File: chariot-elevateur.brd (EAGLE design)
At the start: 123 x 78 mm, 17 parts, among them Q1 BSS138, U1 WIZ820IO

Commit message: end-of-day-commit
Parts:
- moved U1 3.16 mm to (23.0, 52.0)
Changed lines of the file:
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@@
 </layers>
 <board>
-<fusionsync huburn="a.cGVyc29uYWw6dWUyYjVjZTIy" projecturn="a.cGVyc29uYWw6dWUyYjVjZTIyIzIwMTgwOTIxMTUwMjQwNTAx" f3durn="urn:adsk.wipprod:dm.lineage:GSJ6iZW7T-ifCIeOwvPvjQ" pcbguid="b42dcfff-eba5-4b7b-b8d8-54aa01b8e055" lastpulledtime="" lastsyncedchangeguid="7340f699-62a9-14f6-8329-5ece7c968610"/>
+<fusionsync huburn="a.cGVyc29uYWw6dWUyYjVjZTIy" projecturn="a.cGVyc29uYWw6dWUyYjVjZTIyIzIwMTgwOTIxMTUwMjQwNTAx" f3durn="urn:adsk.wipprod:dm.lineage:GSJ6iZW7T-ifCIeOwvPvjQ" pcbguid="b42dcfff-eba5-4b7b-b8d8-54aa01b8e055" lastpulledtime="" lastsyncedchangeguid="24a032fd-58df-3baa-aadd-83ea89c3b94e"/>
 <plain>
 <wire x1="17.5" y1="0" x2="51.5" y2="0" width="0" layer="20"/>
@@
 <attribute name="VALUE" x="79.8" y="41" size="1.27" layer="27" font="vector"/>
 </element>
-<element name="U1" library="wiznet" package="WIZ820" value="WIZ820IO" x="20" y="53" smashed="yes" rot="R180">
-<attribute name="NAME" x="12.38" y="47.158" size="1.6764" layer="25"/>
+<element name="U1" library="wiznet" package="WIZ820" value="WIZ820IO" x="23" y="52" smashed="yes" rot="R180">
+<attribute name="NAME" x="15.38" y="46.158" size="1.6764" layer="25"/>
 </element>
 <element name="ENCODEUR_GAUCHE" library="con-jst" package="GH-04-V" value="JST-04GH-V" x="24" y="6" smashed="yes" rot="R180"/>
@@
 <contactref element="LED2" pad="C"/>
 <wire x1="86.15" y1="33.38" x2="121.71" y2="48.62" width="0" layer="19" extent="1-1"/>
-<wire x1="30.16" y1="53" x2="86.15" y2="33.38" width="0" layer="19" extent="1-1"/>
-<wire x1="30.16" y1="55.54" x2="30.16" y2="53" width="0" layer="19" extent="1-1"/>
-<wire x1="9.84" y1="53" x2="30.16" y2="53" width="0" layer="19" extent="1-1"/>
-<wire x1="33" y1="4.46" x2="9.84" y2="53" width="0" layer="19" extent="1-1"/>
+<wire x1="33.16" y1="52" x2="86.15" y2="33.38" width="0" layer="19" extent="1-1"/>
+<wire x1="33.16" y1="54.54" x2="33.16" y2="52" width="0" layer="19" extent="1-1"/>
+<wire x1="12.84" y1="52" x2="33.16" y2="52" width="0" layer="19" extent="1-1"/>
+<wire x1="33" y1="4.46" x2="12.84" y2="52" width="0" layer="19" extent="1-1"/>
 <wire x1="66.46" y1="12" x2="33" y2="4.46" width="0" layer="19" extent="1-1"/>
 <wire x1="83" y1="18.46" x2="66.46" y2="12" width="0" layer="19" extent="1-1"/>
@@
 <contactref element="U1" pad="VIN2"/>
 <contactref element="U1" pad="VIN1"/>
-<wire x1="9.84" y1="58.08" x2="9.84" y2="55.54" width="0" layer="19" extent="1-1"/>
+<wire x1="12.84" y1="57.08" x2="12.84" y2="54.54" width="0" layer="19" extent="1-1"/>
 </signal>
 <signal name="DYN_VCC">

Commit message: more components
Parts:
- added ENDSTOP: JST-03, con-jst:GH-03-V
- added FUMIGENE: DYNAMIXEL-1X03XL, 1NTech_pinhead:DYNAMIXEL_XL_1X03
- added PHARES_AR, PHARES_AV: JST-05, con-jst:GH-05-V
- added RASPBERRY: JST-06, con-jst:GH-06-V
- added TOF_AR: JST-08, con-jst:GH-08-V
- added VESC: (no value), pinhead:1X03
- moved S3 56.3 mm to (99.0, 75.0), turned to 0 degrees
- moved LED2 39.1 mm to (94.0, 64.0)
- moved LED3 39.1 mm to (94.0, 57.0)
- moved Q1 39.1 mm to (108.0, 57.0)
- moved R2 39.1 mm to (115.0, 56.0)
- moved R3 39.1 mm to (115.0, 61.0)
- moved R4 39.1 mm to (101.0, 56.0)
- moved R5 39.1 mm to (101.0, 61.0)
- moved S1 16.5 mm to (67.0, 23.0), turned to 90 degrees
- moved AX12_AV 15.0 mm to (54.0, 12.0)
- moved PAS_A_PAS 11.0 mm to (67.0, 12.0)
- moved AX12_AR 6.08 mm to (32.0, 13.0), turned to 0 degrees
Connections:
- net DYN_VCC: now also FUMIGENE.VCC
- net GND: now also FUMIGENE.GND

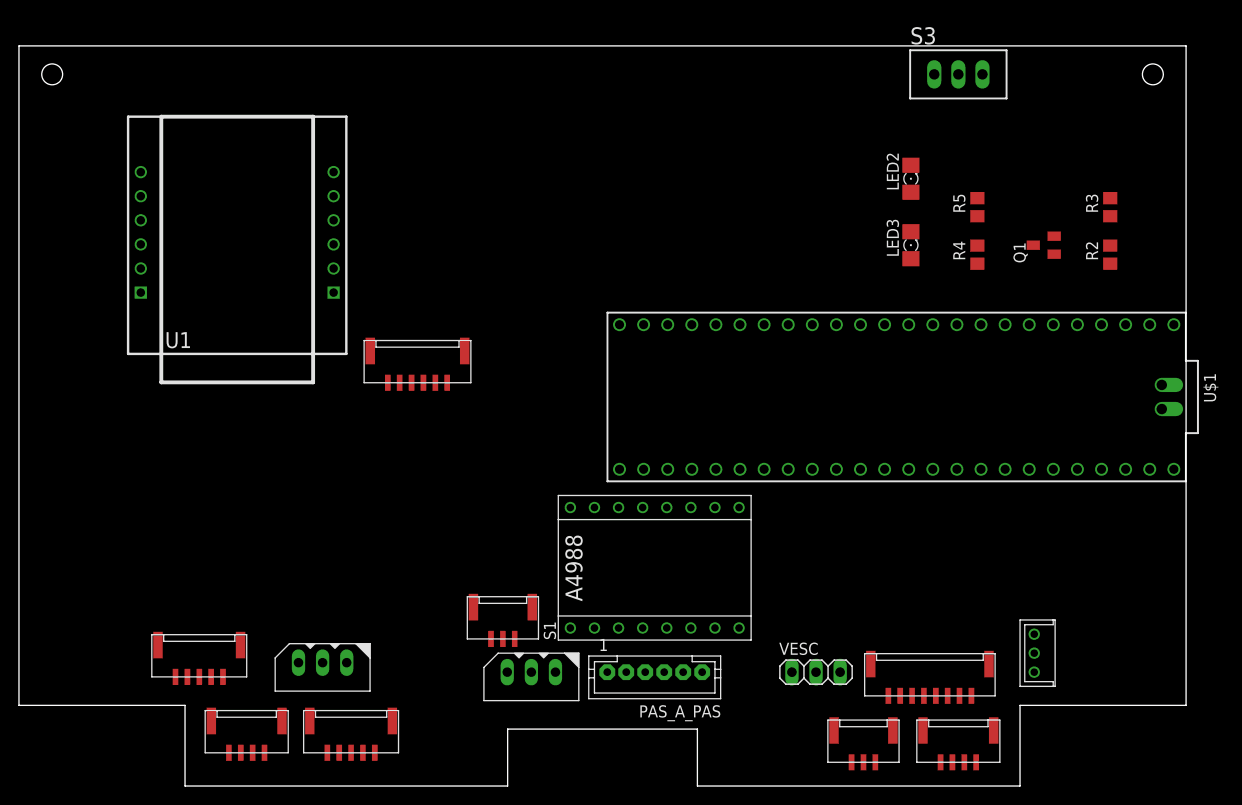
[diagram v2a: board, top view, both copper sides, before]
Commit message: Add power connector
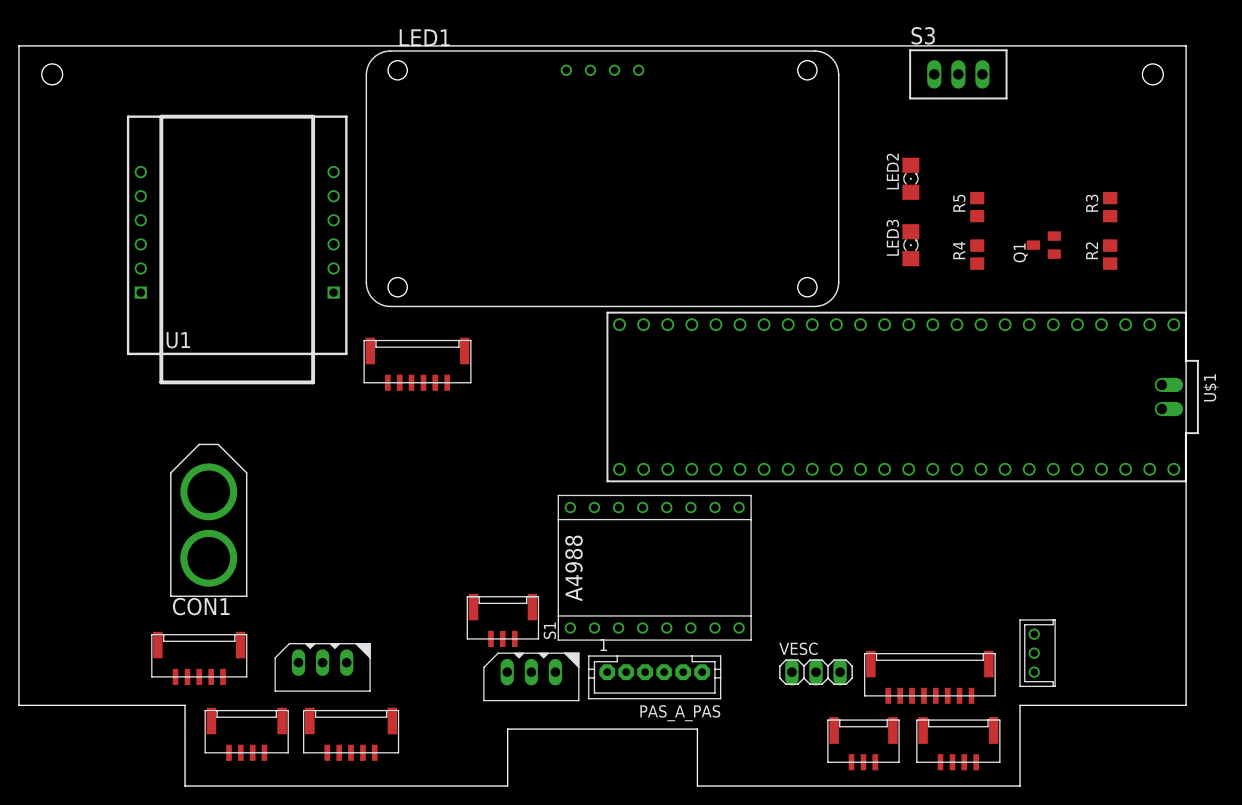
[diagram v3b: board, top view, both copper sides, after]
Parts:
- added CON1: XT-60, con-xt:XT-60
- added LED1: ADAFRUIT_7-SEGMENT-LED, Adafruit-7-segment:0.56"LED_BACKPACK
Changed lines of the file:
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@@
 <drawing>
 <settings>
-<setting alwaysvectorfont="yes"/>
+<setting alwaysvectorfont="no"/>
 <setting verticaltext="up"/>
 </settings>
@@
 <element name="ENDSTOP" library="con-jst" package="GH-03-V" value="JST-03" x="51" y="18" smashed="yes" rot="R180"/>
 <element name="RASPBERRY" library="con-jst" package="GH-06-V" value="JST-06" x="42" y="45" smashed="yes" rot="R180"/>
+<element name="LED1" library="Adafruit-7-segment" package="0.56&quot;LED_BACKPACK" value="ADAFRUIT_7-SEGMENT-LED" x="61.5" y="64" smashed="yes">
+<attribute name="NAME" x="39.91" y="77.97" size="1.778" layer="25"/>
+</element>
+<element name="CON1" library="con-xt" package="XT-60" value="XT-60" x="20" y="28" smashed="yes">
+<attribute name="NAME" x="16.1" y="19.8" size="1.778" layer="21" align="top-left"/>
+</element>
 </elements>
 <signals>
